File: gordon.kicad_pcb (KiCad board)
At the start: 2 copper layers, 70 x 60 mm, 8 parts, among them U1 NUCLEO64-F401RE, U2 SST39SF040

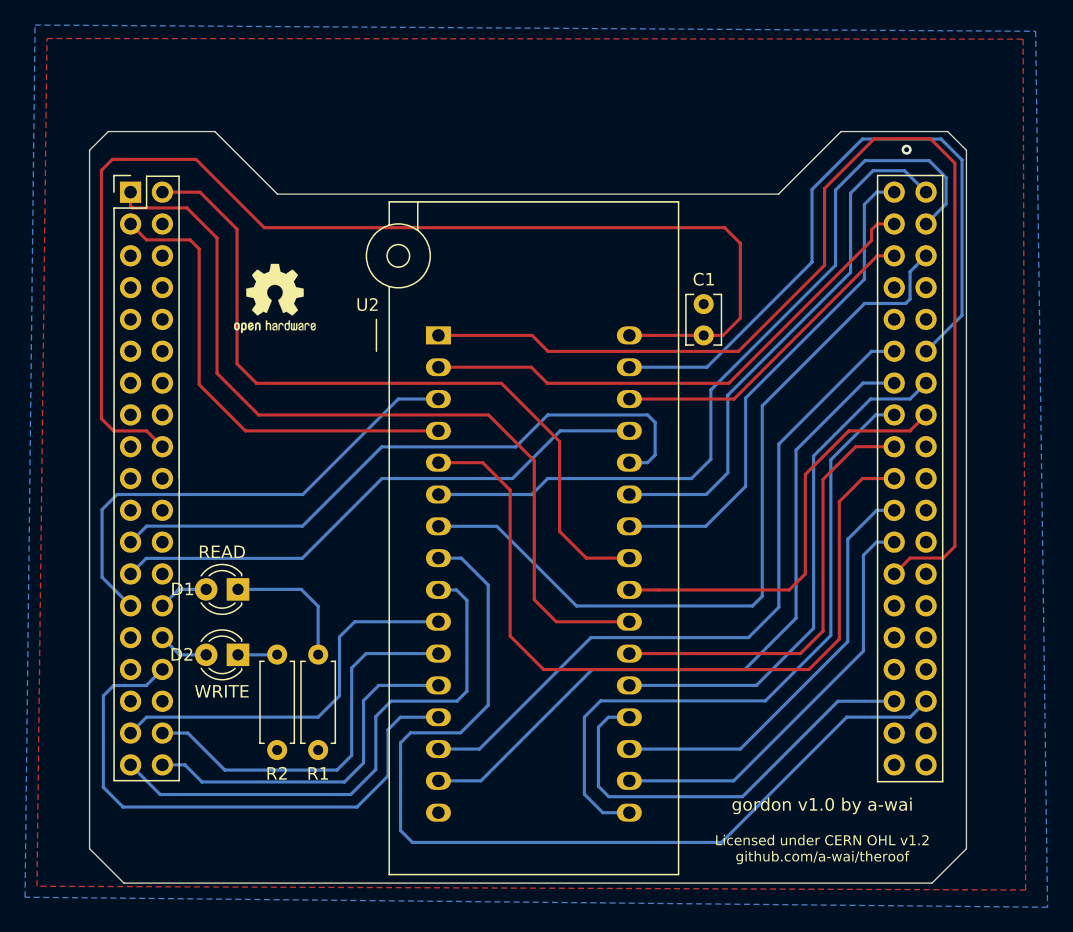
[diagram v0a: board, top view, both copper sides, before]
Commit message: Improve routing of A4 line
Signed-off-by: Arnaud Ferraris <arnaud.ferraris@gmail.com>
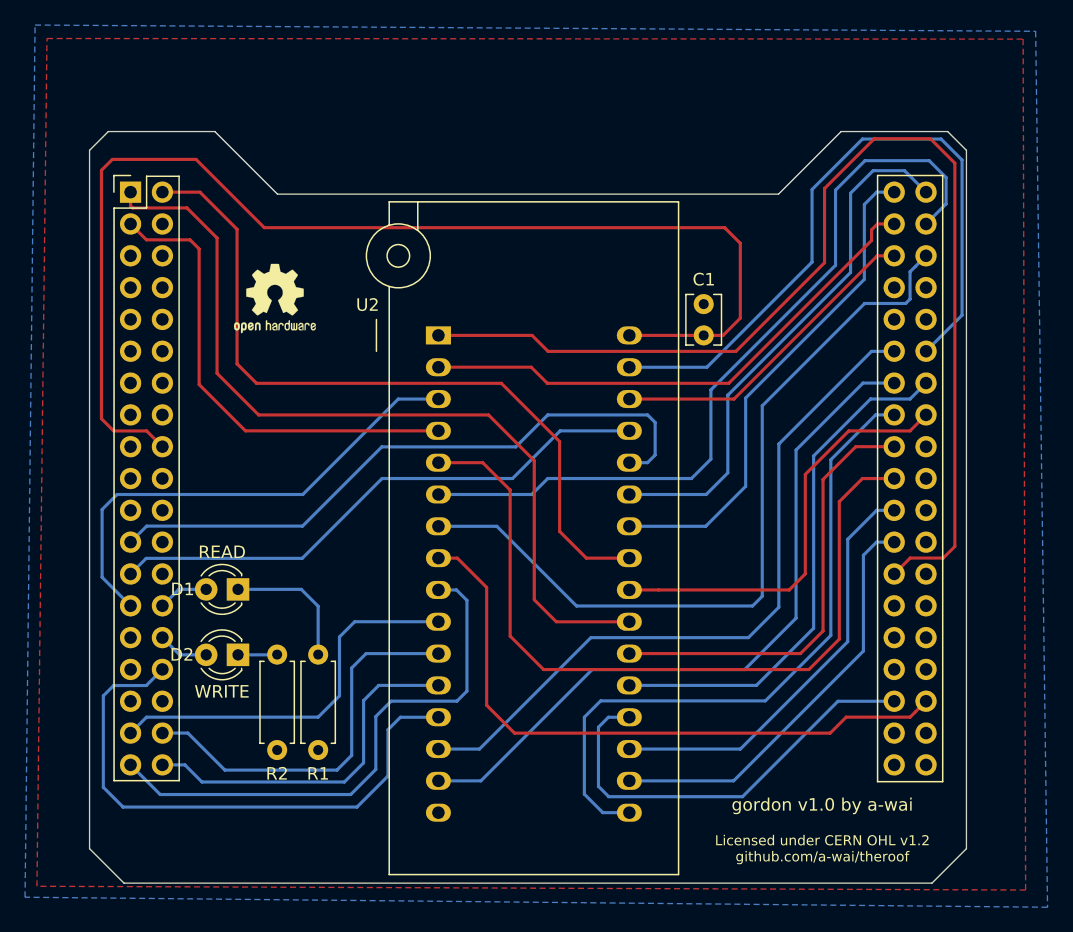
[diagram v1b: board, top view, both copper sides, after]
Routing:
- net /A4: track 76.7 -> 51.3 mm
- net GND: vias 1 -> 0
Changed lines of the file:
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@@
     (thickness 1.6)
     (drawings 14)
-    (tracks 265)
+    (tracks 261)
     (zones 0)
     (modules 8)
@@
     (visible_elements FFFFFF7F)
     (pcbplotparams
-      (layerselection 0x010fc_ffffffff)
-      (usegerberextensions false)
+      (layerselection 0x010e0_ffffffff)
+      (usegerberextensions true)
       (usegerberattributes false)
       (usegerberadvancedattributes false)
@@
       (outputformat 1)
       (mirror false)
-      (drillshape 1)
+      (drillshape 0)
       (scaleselection 1)
-      (outputdirectory ""))
+      (outputdirectory "Gerber/"))
   )
   (net 0 "")
@@
   (gr_line (start 92.25 60) (end 97.25 65) (layer Edge.Cuts) (width 0.05))
   (gr_line (start 83.75 60) (end 92.25 60) (layer Edge.Cuts) (width 0.05))
-  (via (at 147.475 61.45) (size 0.8) (drill 0.4) (layers F.Cu B.Cu) (net 1))
   (segment (start 125.34 76.275) (end 131.275 76.275) (width 0.25) (layer F.Cu) (net 2))
   (segment (start 132.825 76.275) (end 131.275 76.275) (width 0.25) (layer F.Cu) (net 2))
@@
   (segment (start 97.205 101.775) (end 97.225 101.755) (width 0.25) (layer B.Cu) (net 6))
   (segment (start 94.1 101.775) (end 97.205 101.775) (width 0.25) (layer B.Cu) (net 6))
-  (segment (start 111.93 94.055) (end 110.1 94.055) (width 0.25) (layer B.Cu) (net 7))
-  (segment (start 132.7 116.75) (end 108.025 116.75) (width 0.25) (layer B.Cu) (net 7))
-  (segment (start 142.7 106.75) (end 132.7 116.75) (width 0.25) (layer B.Cu) (net 7))
-  (segment (start 147.755 106.75) (end 142.7 106.75) (width 0.25) (layer B.Cu) (net 7))
-  (segment (start 114.075 96.2) (end 111.93 94.055) (width 0.25) (layer B.Cu) (net 7))
-  (segment (start 149.025 105.48) (end 147.755 106.75) (width 0.25) (layer B.Cu) (net 7))
-  (segment (start 108.025 116.75) (end 107.075 115.8) (width 0.25) (layer B.Cu) (net 7))
-  (segment (start 107.075 115.8) (end 107.075 108.8) (width 0.25) (layer B.Cu) (net 7))
-  (segment (start 107.075 108.8) (end 107.875 108) (width 0.25) (layer B.Cu) (net 7))
-  (segment (start 107.875 108) (end 111.875 108) (width 0.25) (layer B.Cu) (net 7))
-  (segment (start 114.075 105.8) (end 114.075 96.2) (width 0.25) (layer B.Cu) (net 7))
-  (segment (start 111.875 108) (end 114.075 105.8) (width 0.25) (layer B.Cu) (net 7))
+  (segment (start 148.175001 106.329999) (end 149.025 105.48) (width 0.25) (layer F.Cu) (net 7))
+  (segment (start 147.755 106.75) (end 148.175001 106.329999) (width 0.25) (layer F.Cu) (net 7))
+  (segment (start 142.65 106.75) (end 147.755 106.75) (width 0.25) (layer F.Cu) (net 7))
+  (segment (start 110.1 94.055) (end 111.605 94.055) (width 0.25) (layer F.Cu) (net 7))
+  (segment (start 113.95 96.4) (end 113.95 105.8) (width 0.25) (layer F.Cu) (net 7))
+  (segment (start 111.605 94.055) (end 113.95 96.4) (width 0.25) (layer F.Cu) (net 7))
+  (segment (start 113.95 105.8) (end 116.175 108.025) (width 0.25) (layer F.Cu) (net 7))
+  (segment (start 141.375 108.025) (end 142.65 106.75) (width 0.25) (layer F.Cu) (net 7))
+  (segment (start 116.175 108.025) (end 141.375 108.025) (width 0.25) (layer F.Cu) (net 7))
   (segment (start 125.34 106.755) (end 123.67 106.755) (width 0.25) (layer B.Cu) (net 8))
   (segment (start 122.875 107.55) (end 122.875 112.275) (width 0.25) (layer B.Cu) (net 8))
@@
   (segment (start 125.34 111.835) (end 133.665 111.835) (width 0.25) (layer B.Cu) (net 10))
   (segment (start 133.665 111.835) (end 144.025 101.475) (width 0.25) (layer B.Cu) (net 10))
-  (segment (start 140.925 70.675) (end 140.925 64.55) (width 0.25) (layer F.Cu) (net 11))
+  (segment (start 147.755 94.05) (end 146.485 95.32) (width 0.25) (layer F.Cu) (net 11))
+  (segment (start 140.925 70.475) (end 140.925 64.55) (width 0.25) (layer F.Cu) (net 11))
+  (segment (start 118.85 77.55) (end 133.85 77.55) (width 0.25) (layer F.Cu) (net 11))
+  (segment (start 133.85 77.55) (end 140.925 70.475) (width 0.25) (layer F.Cu) (net 11))
+  (segment (start 140.925 64.55) (end 144.9 60.575) (width 0.25) (layer F.Cu) (net 11))
+  (segment (start 110.1 76.275) (end 117.575 76.275) (width 0.25) (layer F.Cu) (net 11))
+  (segment (start 117.575 76.275) (end 118.85 77.55) (width 0.25) (layer F.Cu) (net 11))
   (segment (start 144.9 60.575) (end 149.375 60.575) (width 0.25) (layer F.Cu) (net 11))
+  (segment (start 151.325 62.525) (end 151.325 93.125) (width 0.25) (layer F.Cu) (net 11))
   (segment (start 151.325 93.125) (end 150.4 94.05) (width 0.25) (layer F.Cu) (net 11))
-  (segment (start 134.05 77.55) (end 140.925 70.675) (width 0.25) (layer F.Cu) (net 11))
-  (segment (start 118.85 77.55) (end 134.05 77.55) (width 0.25) (layer F.Cu) (net 11))
-  (segment (start 147.755 94.05) (end 146.485 95.32) (width 0.25) (layer F.Cu) (net 11))
-  (segment (start 110.1 76.275) (end 117.575 76.275) (width 0.25) (layer F.Cu) (net 11))
+  (segment (start 150.4 94.05) (end 147.755 94.05) (width 0.25) (layer F.Cu) (net 11))
   (segment (start 149.375 60.575) (end 151.325 62.525) (width 0.25) (layer F.Cu) (net 11))
-  (segment (start 151.325 62.525) (end 151.325 93.125) (width 0.25) (layer F.Cu) (net 11))
-  (segment (start 117.575 76.275) (end 118.85 77.55) (width 0.25) (layer F.Cu) (net 11))
-  (segment (start 140.925 64.55) (end 144.9 60.575) (width 0.25) (layer F.Cu) (net 11))
-  (segment (start 150.4 94.05) (end 147.755 94.05) (width 0.25) (layer F.Cu) (net 11))
   (segment (start 145.085 90.24) (end 146.485 90.24) (width 0.25) (layer B.Cu) (net 12))
   (segment (start 125.34 109.295) (end 134.205 109.295) (width 0.25) (layer B.Cu) (net 12))
